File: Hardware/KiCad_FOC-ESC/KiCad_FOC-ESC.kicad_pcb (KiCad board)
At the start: 6 copper layers, 51 x 46 mm, 70 parts, among them IC1 TCAN3414DDFR, IC2 TSC1801BILT, IC3 TSC1801BILT, IC4 TSC1801BILT, IC5 REF2030AIDDCR, IC6 MA702GQ-P, IC901 DRV8320SRTVR, J1 Conn_01x06, J2 Prog, Q1 NTTFS5D6N08XLTAG, Q2 NTTFS5D6N08XLTAG, Q3 NTTFS5D6N08XLTAG, Q4 NTTFS5D6N08XLTAG, Q5 NTTFS5D6N08XLTAG, Q6 NTTFS5D6N08XLTAG, U1 STM32G473RCTx, U3 MT6701CT, U802 ZLDO1117Q, Y1 ASDDV-16.000MHZ-LR-T

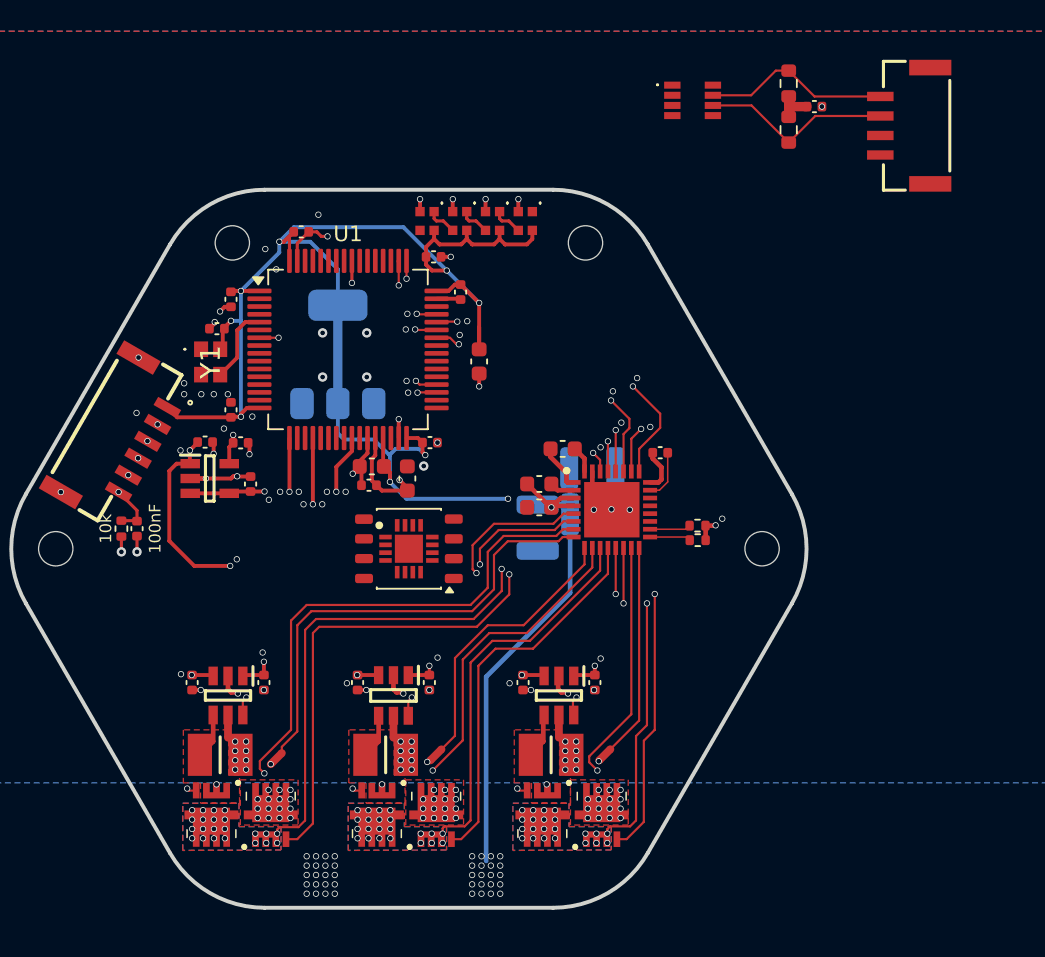
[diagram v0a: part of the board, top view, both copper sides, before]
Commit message: init FOC-ESC connections
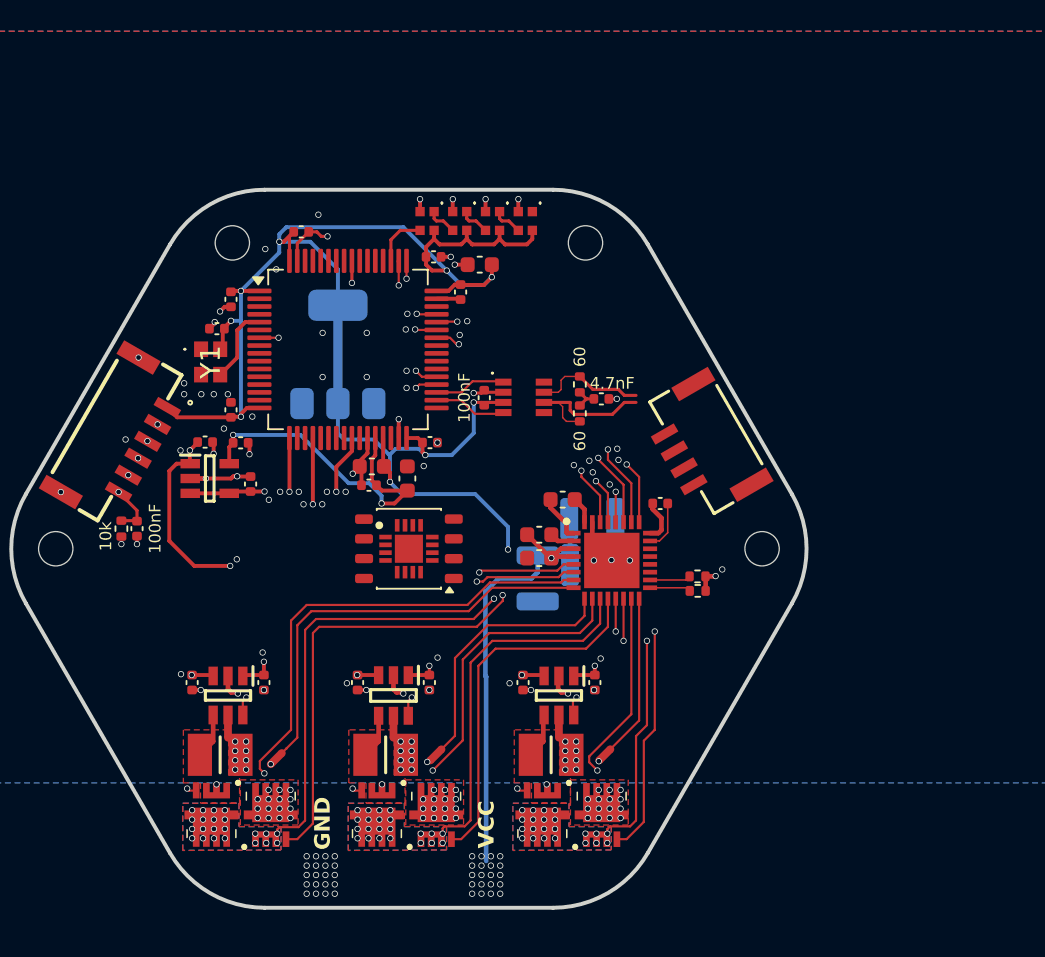
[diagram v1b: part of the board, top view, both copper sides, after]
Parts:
- added C22: 100nF, Capacitor_SMD:C_0402_1005Metric, F.Cu at (131.3, 73.6)
- R2, R3: footprint Resistor_SMD:R_0603_1608Metric -> Resistor_SMD:R_0402_1005Metric
- moved J1 24.9 mm to (143.9, 77.5), turned to 120 degrees
- moved R2 23.5 mm to (137.4, 72.8)
- moved C21 23.2 mm to (138.8, 73.7)
- moved R3 22.6 mm to (137.4, 74.6)
- moved IC1 21.9 mm to (133.8, 73.6)
- moved C1 6.20 mm to (131.0, 65.1), turned to 180 degrees
- moved C110 3.25 mm to (138.2, 84.4)
- moved C116 3.25 mm to (138.2, 81.4)
- moved C901 3.25 mm to (142.6, 80.4)
- moved C902 3.25 mm to (134.8, 82.4)
- moved C903 3.25 mm to (134.8, 83.9)
- moved C904 3.25 mm to (136.3, 80.2)
- moved C122 3.25 mm to (134.7, 85.2)
- moved IC901 3.25 mm to (139.4, 84.0)
- moved R901 3.25 mm to (144.9, 85.1)
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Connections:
- net CANH renamed CAN+
- net CANL renamed CAN-
- U1 pad 34: unconnected-(U1-PB12-Pad34) -> CANRX
- U1 pad 35: INLC -> CANTX
- U1 pad 37: unconnected-(U1-PB15-Pad37) -> INLC
- U1 pad 51: unconnected-(U1-PA15-Pad51) -> DebugLED_IN
- U1 pad 57: CAN_STB -> unconnected-(U1-PB4-Pad57)
- U1 pad 58: CAN_SHDNVIO -> unconnected-(U1-PB5-Pad58)
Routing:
- net +3V: track 8.28 -> 21.1 mm
- net +3V3: track 169.9 -> 175.8 mm, vias 15 -> 16
- net INLC: track 16.0 -> 21.8 mm
- net CAN+: track 12.2 -> 7.22 mm
- net CANRX: track 0.00 -> 4.67 mm
- net CANTX: track 0.00 -> 4.59 mm
- net GHA: track 40.7 -> 36.1 mm
- net INLB: track 18.6 -> 22.3 mm
- net DebugLED_IN: track 0.00 -> 3.47 mm
- net SHA: track 38.8 -> 35.4 mm
- net GLC: track 22.1 -> 18.8 mm
- net GHC: track 22.5 -> 19.3 mm
- net /FETs/DRV8320S_1/SPC: track 13.7 -> 10.4 mm
- net SHC: track 21.6 -> 18.5 mm
- net GLA: track 38.9 -> 36.2 mm
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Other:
- board text added: "A"
- board text added: "B"
- board text added: "C"
- board text added: "GND"
- board text added: "VCC"
- board text added: "add humongous Caps."

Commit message: added CAN
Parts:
- moved J1 3.95 mm to (142.0, 74.0)
- moved R3 0.67 mm to (137.0, 74.1), turned to 180 degrees
- moved R2 0.52 mm to (137.0, 73.1), turned to 0 degrees
- moved C21 0.13 mm to (138.9, 73.6)
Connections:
- J1 pad 1: unconnected-(J1-Pin_1-Pad1) -> +3V3
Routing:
- net +3V3: track 175.8 -> 187.8 mm, vias 16 -> 17
- net CAN-: track 10.1 -> 7.12 mm
- net CAN+: track 7.22 -> 6.49 mm
- net GND: track 38.8 -> 38.7 mm, vias 122 -> 129
- removed copper zone on B.Cu, net VCC
